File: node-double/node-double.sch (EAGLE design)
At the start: 29 parts, among them IC1 TP4056, IC3 24C02, U1 ATMEGA328P_TQFP, U2 3.3V/150mA

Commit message: Revert "Router PCB"
This reverts commit 5cfdc418179729a7dd419c7a517ca3d373416e11.
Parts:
- added LED1, LED2: (no value), led:LEDSML0805
- added R2, R3: 1K, resistor:R-US_R0603
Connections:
- new net N$1: LED1.C, R2.1
- new net N$2: LED2.C, R3.1
- net D4: now also LED1.A
- net D6: now also LED2.A
- net GND: now also R2.2, R3.2
- net VCC: no longer IC1.CE
- net VIN: now also IC1.CE
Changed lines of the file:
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@@
 <?xml version="1.0" encoding="utf-8"?>
 <!DOCTYPE eagle SYSTEM "eagle.dtd">
-<eagle version="8.3.2">
+<eagle version="9.0.0">
 <drawing>
 <settings>
@@
 <part name="GND10" library="SparkFun-PowerSymbols" deviceset="GND" device=""/>
 <part name="U$2" library="pinhead" library_urn="urn:adsk.eagle:library:325" deviceset="PINHD-2X4" device="" package3d_urn="urn:adsk.eagle:package:22461/2"/>
+<part name="LED1" library="led" library_urn="urn:adsk.eagle:library:259" deviceset="LED" device="SML0805" package3d_urn="urn:adsk.eagle:package:15830/1"/>
+<part name="LED2" library="led" library_urn="urn:adsk.eagle:library:259" deviceset="LED" device="SML0805" package3d_urn="urn:adsk.eagle:package:15830/1"/>
+<part name="R2" library="resistor" library_urn="urn:adsk.eagle:library:348" deviceset="R-US_" device="R0603" package3d_urn="urn:adsk.eagle:package:26057/1" value="1K">
+<attribute name="MF" value=""/>
+<attribute name="MPN" value=""/>
+<attribute name="OC_FARNELL" value="unknown"/>
+</part>
+<part name="R3" library="resistor" library_urn="urn:adsk.eagle:library:348" deviceset="R-US_" device="R0603" package3d_urn="urn:adsk.eagle:package:26057/1" value="1K">
+<attribute name="MF" value=""/>
+<attribute name="MPN" value=""/>
+<attribute name="OC_FARNELL" value="unknown"/>
+</part>
+<part name="GND12" library="SparkFun-PowerSymbols" deviceset="GND" device=""/>
 </parts>
 <sheets>
@@
 <instance part="GND10" gate="1" x="195.58" y="-48.26"/>
 <instance part="U$2" gate="A" x="91.44" y="-7.62"/>
+<instance part="LED1" gate="G$1" x="93.98" y="53.34" rot="R90"/>
+<instance part="LED2" gate="G$1" x="93.98" y="48.26" rot="R90"/>
+<instance part="R2" gate="G$1" x="104.14" y="53.34">
+<attribute name="OC_FARNELL" x="104.14" y="53.34" size="1.778" layer="96" rot="R90" display="off"/>
+<attribute name="MF" x="104.14" y="53.34" size="1.778" layer="96" rot="R90" display="off"/>
+<attribute name="MPN" x="104.14" y="53.34" size="1.778" layer="96" rot="R90" display="off"/>
+</instance>
+<instance part="R3" gate="G$1" x="104.14" y="48.26">
+<attribute name="OC_FARNELL" x="104.14" y="48.26" size="1.778" layer="96" rot="R90" display="off"/>
+<attribute name="MF" x="104.14" y="48.26" size="1.778" layer="96" rot="R90" display="off"/>
+<attribute name="MPN" x="104.14" y="48.26" size="1.778" layer="96" rot="R90" display="off"/>
+</instance>
+<instance part="GND12" gate="1" x="111.76" y="43.18"/>
 </instances>
 <busses>
@@
 <wire x1="101.6" y1="-10.16" x2="96.52" y2="-10.16" width="0.1524" layer="91"/>
 <label x="101.6" y="-10.16" size="1.778" layer="95"/>
+</segment>
+<segment>
+<pinref part="R3" gate="G$1" pin="2"/>
+<pinref part="GND12" gate="1" pin="GND"/>
+<wire x1="109.22" y1="48.26" x2="111.76" y2="48.26" width="0.1524" layer="91"/>
+<wire x1="111.76" y1="48.26" x2="111.76" y2="45.72" width="0.1524" layer="91"/>
+<pinref part="R2" gate="G$1" pin="2"/>
+<wire x1="109.22" y1="53.34" x2="111.76" y2="53.34" width="0.1524" layer="91"/>
+<wire x1="111.76" y1="53.34" x2="111.76" y2="48.26" width="0.1524" layer="91"/>
+<junction x="111.76" y="48.26"/>
 </segment>
 </net>
@@
 <pinref part="R5" gate="G$1" pin="2"/>
 <pinref part="SUPPLY3" gate="G$1" pin="VCC"/>
-<pinref part="IC1" gate="G$1" pin="CE"/>
-<wire x1="149.86" y1="88.9" x2="149.86" y2="99.06" width="0.1524" layer="91"/>
-<wire x1="149.86" y1="99.06" x2="154.94" y2="99.06" width="0.1524" layer="91"/>
 <junction x="160.02" y="99.06"/>
 <pinref part="R4" gate="G$1" pin="2"/>
-<junction x="154.94" y="99.06"/>
 <wire x1="154.94" y1="99.06" x2="160.02" y2="99.06" width="0.1524" layer="91"/>
 </segment>
@@
 <segment>
 <pinref part="U1" gate="U$1" pin="PD4(XCK/T0)"/>
-<wire x1="55.88" y1="53.34" x2="68.58" y2="53.34" width="0.1524" layer="91"/>
 <label x="68.58" y="53.34" size="1.778" layer="95" xref="yes"/>
+<pinref part="LED1" gate="G$1" pin="A"/>
+<wire x1="91.44" y1="53.34" x2="55.88" y2="53.34" width="0.1524" layer="91"/>
 </segment>
 </net>
@@
 <segment>
 <pinref part="U1" gate="U$1" pin="PD6(AIN0)"/>
-<wire x1="55.88" y1="48.26" x2="68.58" y2="48.26" width="0.1524" layer="91"/>
 <label x="68.58" y="48.26" size="1.778" layer="95" xref="yes"/>
+<pinref part="LED2" gate="G$1" pin="A"/>
+<wire x1="91.44" y1="48.26" x2="55.88" y2="48.26" width="0.1524" layer="91"/>
 </segment>
 </net>
@@
 <segment>
 <pinref part="IC1" gate="G$1" pin="VCC"/>
-<wire x1="121.92" y1="81.28" x2="116.84" y2="81.28" width="0.1524" layer="91"/>
+<wire x1="121.92" y1="81.28" x2="119.38" y2="81.28" width="0.1524" layer="91"/>
 <label x="116.84" y="81.28" size="1.778" layer="95" rot="R180" xref="yes"/>
 <pinref part="C2" gate="G$1" pin="1"/>
+<wire x1="119.38" y1="81.28" x2="116.84" y2="81.28" width="0.1524" layer="91"/>
 <wire x1="121.92" y1="81.28" x2="121.92" y2="76.2" width="0.1524" layer="91"/>
 <junction x="121.92" y="81.28"/>
+<pinref part="IC1" gate="G$1" pin="CE"/>
+<wire x1="149.86" y1="88.9" x2="149.86" y2="96.52" width="0.1524" layer="91"/>
+<wire x1="149.86" y1="96.52" x2="119.38" y2="96.52" width="0.1524" layer="91"/>
+<wire x1="119.38" y1="96.52" x2="119.38" y2="81.28" width="0.1524" layer="91"/>
+<junction x="119.38" y="81.28"/>
 </segment>
 <segment>
@@
 </segment>
 </net>
+<net name="N$1" class="0">
+<segment>
+<pinref part="LED1" gate="G$1" pin="C"/>
+<pinref part="R2" gate="G$1" pin="1"/>
+</segment>
+</net>
+<net name="N$2" class="0">
+<segment>
+<pinref part="LED2" gate="G$1" pin="C"/>
+<pinref part="R3" gate="G$1" pin="1"/>
+</segment>
+</net>

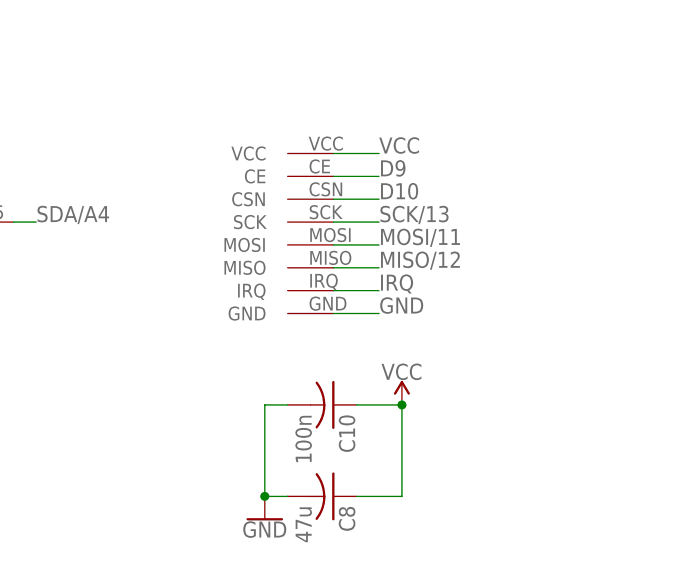
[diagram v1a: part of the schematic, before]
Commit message: Node: Adding interrupt pin
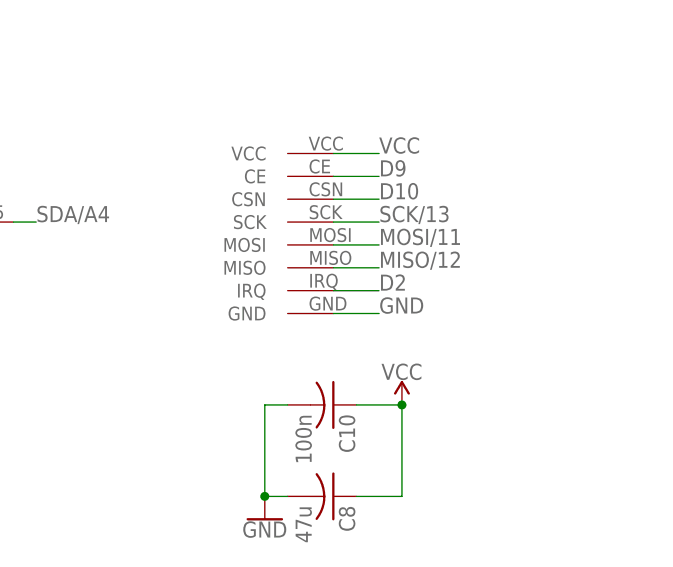
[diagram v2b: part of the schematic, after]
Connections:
- removed net IRQ: U$1.IRQ
- net D2: now also U$1.IRQ
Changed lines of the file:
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@@
 <label x="68.58" y="58.42" size="1.778" layer="95" xref="yes"/>
+</segment>
+<segment>
+<pinref part="U$1" gate="G$1" pin="IRQ"/>
+<wire x1="208.28" y1="-22.86" x2="203.2" y2="-22.86" width="0.1524" layer="91"/>
+<label x="208.28" y="-22.86" size="1.778" layer="95"/>
 </segment>
 </net>
@@
 </segment>
 </net>
-<net name="IRQ" class="0">
-<segment>
-<pinref part="U$1" gate="G$1" pin="IRQ"/>
-<wire x1="208.28" y1="-22.86" x2="203.2" y2="-22.86" width="0.1524" layer="91"/>
-<label x="208.28" y="-22.86" size="1.778" layer="95"/>
-</segment>
-</net>

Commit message: Scratch progress
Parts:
- removed C4: 10u, resistor:C-USC0603
- removed IC3: 24C02, microchip:24C02ASN
- C1, C2, C3, C5, C7, C9: device resistor:C-USC0603 -> Nordic_nRF:CAPACITOR_0603_L
- C6: value 0.1u -> 100n; device resistor:C-USC0603 -> Nordic_nRF:CAPACITOR_0603_L
- R1, R14, R15, R2, R3, R4, R5, R6: device resistor:R-US_R0603 -> SparkFun-Resistors:RESISTOR0603
- R10, R11: value 100k -> 100K; device resistor:R-US_R0603 -> SparkFun-Resistors:RESISTOR0603
- R12, R8: value 470k -> 470K; device resistor:R-US_R0603 -> SparkFun-Resistors:RESISTOR0603
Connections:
- net D3: no longer IC3.WP
- net D7: now also IC1.STDBY, R5.1; no longer IC1.CHRG, R4.1
- net D8: now also IC1.CHRG, R4.1; no longer IC1.STDBY, R5.1
- net GND: no longer C4.2, IC3.A0, IC3.A1, IC3.A2, IC3.GND
- net SCL/A5: no longer IC3.SCL
- net SDA/A4: no longer IC3.SDA
- net VBAT: no longer C4.1
- net VCC: no longer IC3.VCC

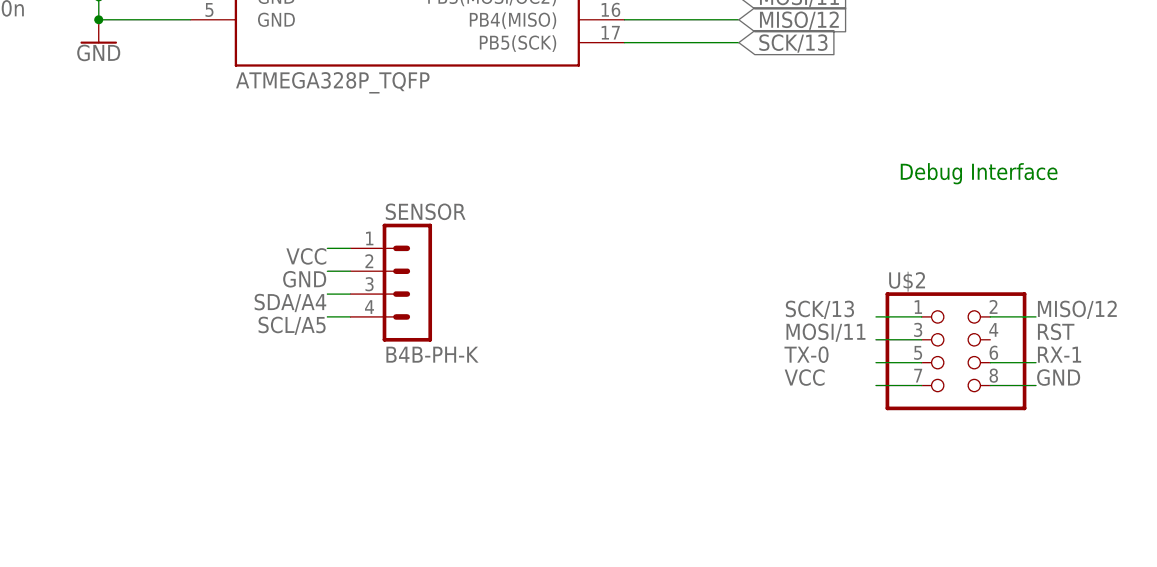
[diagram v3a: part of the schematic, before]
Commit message: Post-ramp circuit fixes
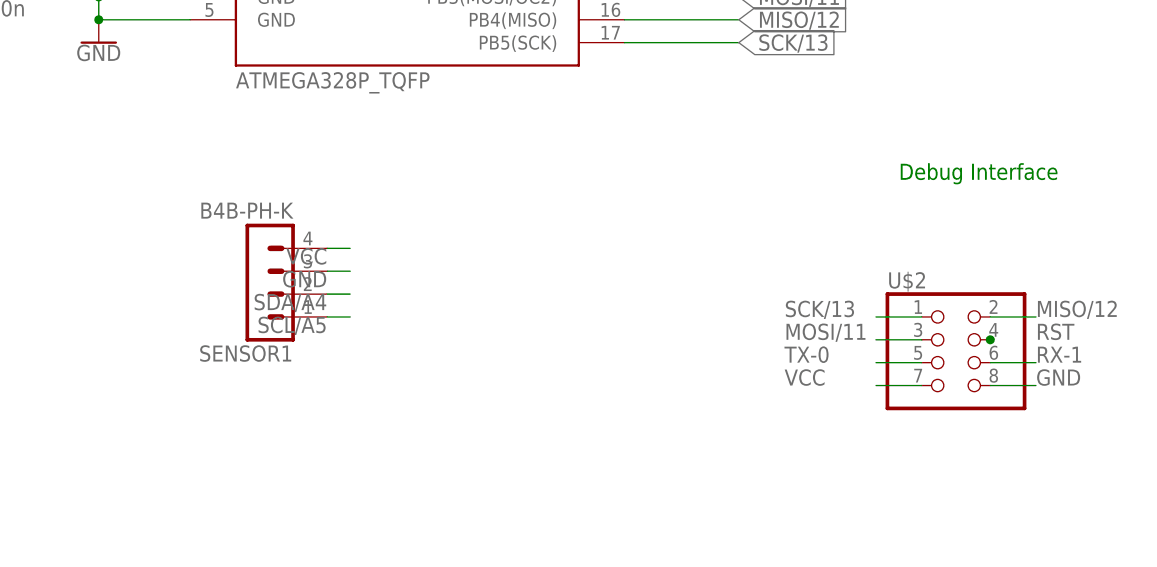
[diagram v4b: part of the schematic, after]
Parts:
- removed SENSOR: B4B-PH-K, con-jst-ph:B4B-PH-K
- added SENSOR1: B4B-PH-K, con-jst-ph:B4B-PH-K
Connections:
- net GND: now also SENSOR1.3; no longer SENSOR.2
- net SCL/A5: now also SENSOR1.1; no longer SENSOR.4
- net SDA/A4: now also SENSOR1.2; no longer SENSOR.3
- net VCC: now also SENSOR1.4; no longer SENSOR.1
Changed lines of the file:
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@@
 <?xml version="1.0" encoding="utf-8"?>
 <!DOCTYPE eagle SYSTEM "eagle.dtd">
-<eagle version="9.0.0">
+<eagle version="9.1.1">
 <drawing>
 <settings>
@@
 <part name="J_BATT" library="con-jst-ph" deviceset="B2B-PH-K" device="" value=""/>
 <part name="J_SOLAR" library="con-jst-ph" deviceset="B2B-PH-K" device="" value=""/>
-<part name="SENSOR" library="con-jst-ph" deviceset="B4B-PH-K" device=""/>
 <part name="U$1" library="ebyte" deviceset="ML01S" device="SMD-SOM"/>
 <part name="SUPPLY7" library="SparkFun-PowerSymbols" deviceset="VCC" device=""/>
@@
 </part>
 <part name="GND12" library="SparkFun-PowerSymbols" deviceset="GND" device=""/>
+<part name="SENSOR1" library="con-jst-ph" deviceset="B4B-PH-K" device=""/>
 </parts>
 <sheets>
@@
 <instance part="J_BATT" gate="G$1" x="223.52" y="58.42"/>
 <instance part="J_SOLAR" gate="G$1" x="200.66" y="58.42"/>
-<instance part="SENSOR" gate="G$1" x="30.48" y="0"/>
 <instance part="U$1" gate="G$1" x="226.06" y="-20.32"/>
 <instance part="SUPPLY7" gate="G$1" x="210.82" y="-35.56"/>
@@
 </instance>
 <instance part="GND12" gate="1" x="111.76" y="43.18"/>
+<instance part="SENSOR1" gate="G$1" x="17.78" y="2.54" rot="R180"/>
 </instances>
 <busses>
@@
 </segment>
 <segment>
-<pinref part="SENSOR" gate="G$1" pin="2"/>
 <wire x1="22.86" y1="2.54" x2="25.4" y2="2.54" width="0.1524" layer="91"/>
 <label x="22.86" y="2.54" size="1.778" layer="95" rot="R180"/>
+<pinref part="SENSOR1" gate="G$1" pin="3"/>
 </segment>
 <segment>
@@
 </segment>
 <segment>
-<pinref part="SENSOR" gate="G$1" pin="1"/>
 <wire x1="22.86" y1="5.08" x2="25.4" y2="5.08" width="0.1524" layer="91"/>
 <label x="22.86" y="5.08" size="1.778" layer="95" rot="R180"/>
+<pinref part="SENSOR1" gate="G$1" pin="4"/>
 </segment>
 <segment>
@@
 <pinref part="U$2" gate="A" pin="4"/>
 <label x="101.6" y="-5.08" size="1.778" layer="95"/>
+<junction x="96.52" y="-5.08"/>
 </segment>
 </net>
@@
 </segment>
 <segment>
-<pinref part="SENSOR" gate="G$1" pin="4"/>
 <wire x1="22.86" y1="-2.54" x2="25.4" y2="-2.54" width="0.1524" layer="91"/>
 <label x="22.86" y="-2.54" size="1.778" layer="95" rot="R180"/>
+<pinref part="SENSOR1" gate="G$1" pin="1"/>
 </segment>
 </net>
@@
 </segment>
 <segment>
-<pinref part="SENSOR" gate="G$1" pin="3"/>
 <wire x1="22.86" y1="0" x2="25.4" y2="0" width="0.1524" layer="91"/>
 <label x="22.86" y="0" size="1.778" layer="95" rot="R180"/>
-</segment>
-</net>
+<pinref part="SENSOR1" gate="G$1" pin="2"/>
+</segment>
+</net>
